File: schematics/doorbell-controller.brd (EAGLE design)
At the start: 114.3 x 100 mm, 7 parts, among them Q1 BC557

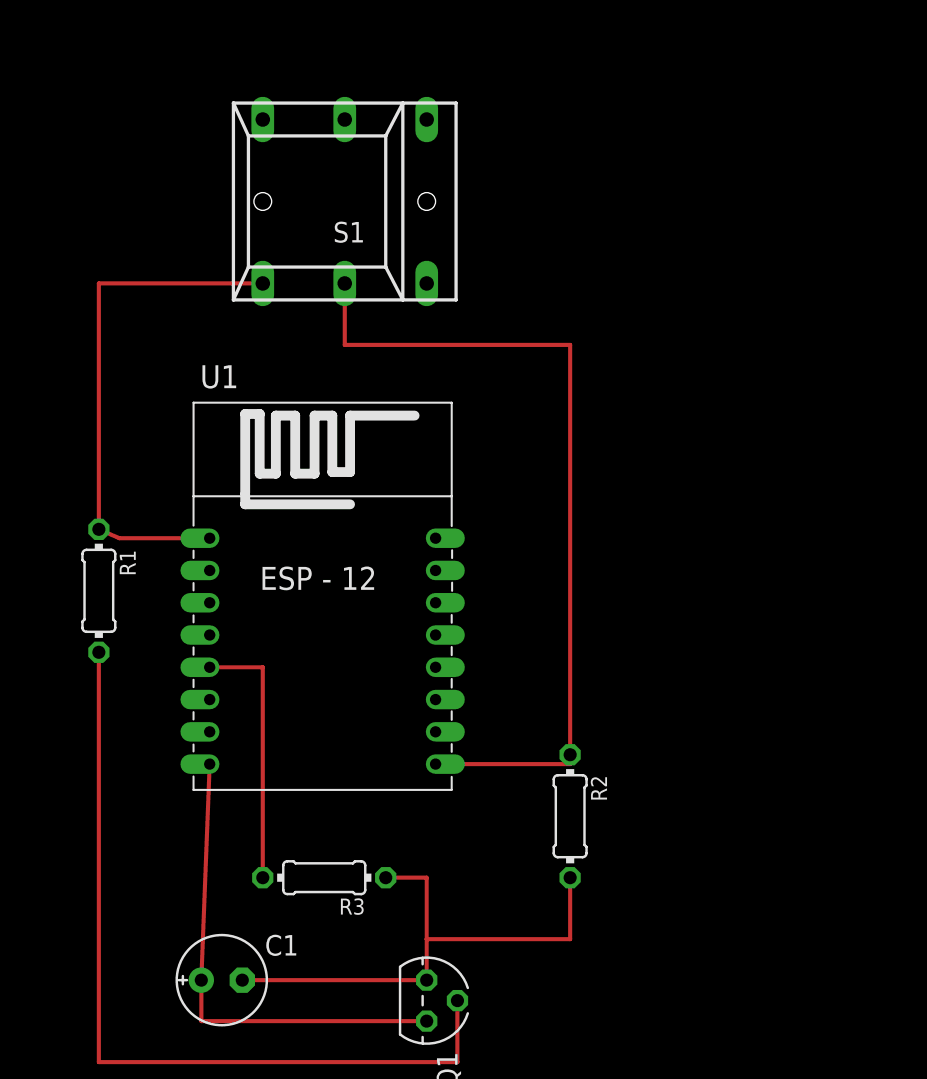
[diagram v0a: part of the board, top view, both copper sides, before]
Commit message: Added LEDs to schematics; Replaces button with Clamp
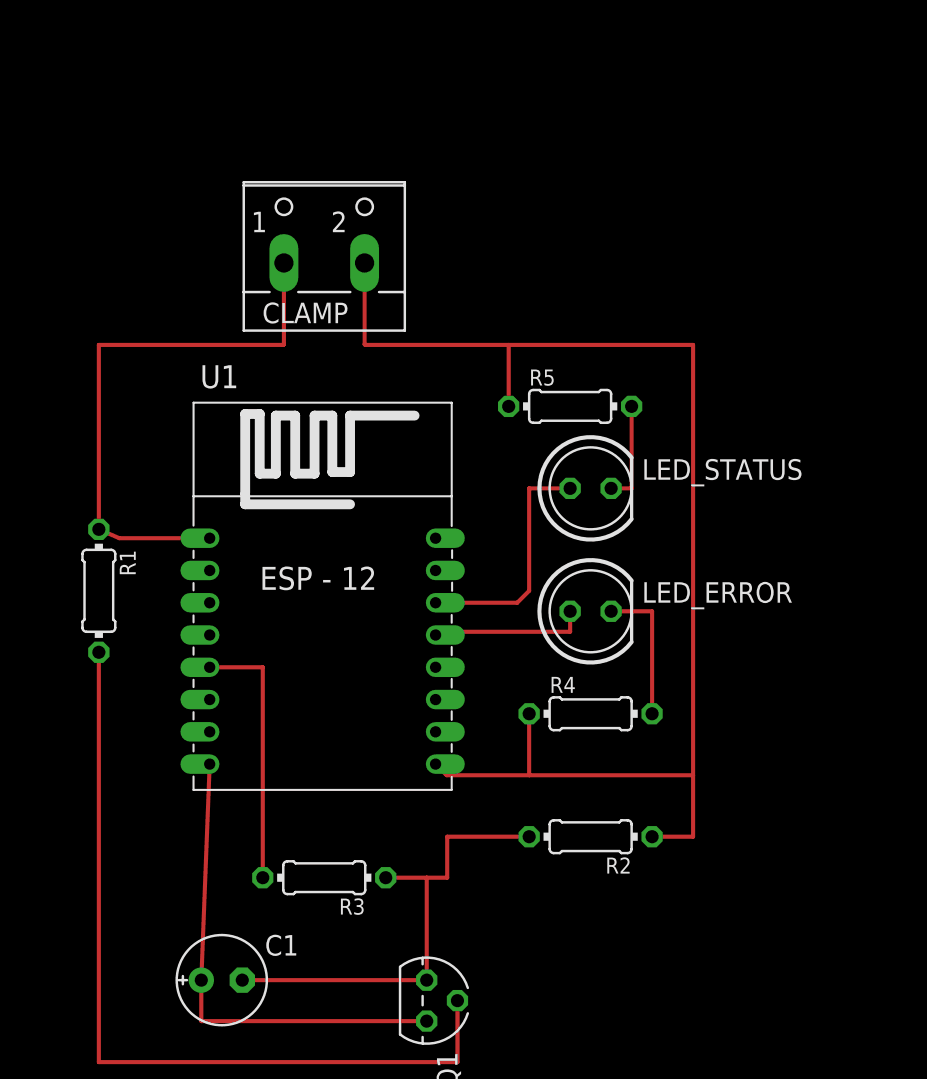
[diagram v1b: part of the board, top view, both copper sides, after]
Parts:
- removed S1: (no value), switch:REKN
- added CLAMP: (no value), con-wago-500:W237-102
- added LED_ERROR, LED_STATUS: (no value), led:LED5MM
- added R4, R5: 470, rcl:0204/7
- moved R2 1.80 mm to (66.0, 38.1), turned to 180 degrees
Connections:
- new net N$1: LED_STATUS.A, U1.GPIO5
- new net N$4: LED_ERROR.A, U1.GPIO4
- new net N$6: LED_ERROR.K, R4.2
- new net N$7: LED_STATUS.K, R5.2
- net GND: now also CLAMP.2, R4.1, R5.1; no longer S1.1A
- net RST: now also CLAMP.1; no longer S1.0A
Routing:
- net GND: track 52.1 -> 82.3 mm
- net N$1: track 0.00 -> 15.0 mm
- net N$4: track 0.00 -> 9.69 mm
- net N$6: track 0.00 -> 8.89 mm
- net N$7: track 0.00 -> 6.35 mm
- net N$5: track 33.0 -> 29.2 mm
- net RST: track 32.4 -> 34.9 mm
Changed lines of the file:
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@@
 <attribute name="SPICEPREFIX" value="R" x="35.56" y="53.34" size="1.778" layer="27" rot="R270" display="off"/>
 </element>
-<element name="R2" library="rcl" library_urn="urn:adsk.eagle:library:334" package="0204/7" package3d_urn="urn:adsk.eagle:package:23498/1" value="22k" x="64.77" y="39.37" rot="R270">
-<attribute name="SPICEPREFIX" value="R" x="64.77" y="39.37" size="1.778" layer="27" rot="R270" display="off"/>
+<element name="R2" library="rcl" library_urn="urn:adsk.eagle:library:334" package="0204/7" package3d_urn="urn:adsk.eagle:package:23498/1" value="22k" x="66.04" y="38.1" rot="R180">
+<attribute name="SPICEPREFIX" value="R" x="66.04" y="38.1" size="1.778" layer="27" rot="R180" display="off"/>
 </element>
 <element name="R3" library="rcl" library_urn="urn:adsk.eagle:library:334" package="0204/7" package3d_urn="urn:adsk.eagle:package:23498/1" value="470" x="49.53" y="35.56" rot="R180">
 <attribute name="SPICEPREFIX" value="R" x="49.53" y="35.56" size="1.778" layer="27" rot="R180" display="off"/>
 </element>
-<element name="S1" library="switch" library_urn="urn:adsk.eagle:library:380" package="REKN" package3d_urn="urn:adsk.eagle:package:27692/1" value="" x="50.8" y="77.47" rot="R180"/>
 <element name="U1" library="esp8266modules" package="ESP12-TR" value="" x="49.53" y="50.8"/>
+<element name="LED_STATUS" library="led" library_urn="urn:adsk.eagle:library:259" package="LED5MM" package3d_urn="urn:adsk.eagle:package:15799/2" value="" x="66.04" y="59.69"/>
+<element name="LED_ERROR" library="led" library_urn="urn:adsk.eagle:library:259" package="LED5MM" package3d_urn="urn:adsk.eagle:package:15799/2" value="" x="66.04" y="52.07"/>
+<element name="R4" library="rcl" library_urn="urn:adsk.eagle:library:334" package="0204/7" package3d_urn="urn:adsk.eagle:package:23498/1" value="470" x="66.04" y="45.72">
+<attribute name="SPICEPREFIX" value="R" x="66.04" y="45.72" size="1.778" layer="27" display="off"/>
+</element>
+<element name="R5" library="rcl" library_urn="urn:adsk.eagle:library:334" package="0204/7" package3d_urn="urn:adsk.eagle:package:23498/1" value="470" x="64.77" y="64.77">
+<attribute name="SPICEPREFIX" value="R" x="64.77" y="64.77" size="1.778" layer="27" display="off"/>
+</element>
+<element name="CLAMP" library="con-wago-500" library_urn="urn:adsk.eagle:library:195" package="W237-102" package3d_urn="urn:adsk.eagle:package:10688/1" value="" x="49.53" y="74.93">
+<attribute name="MF" value="" x="49.53" y="74.93" size="1.778" layer="27" display="off"/>
+<attribute name="MPN" value="237-102" x="49.53" y="74.93" size="1.778" layer="27" display="off"/>
+<attribute name="OC_FARNELL" value="unknown" x="49.53" y="74.93" size="1.778" layer="27" display="off"/>
+<attribute name="OC_NEWARK" value="70K9898" x="49.53" y="74.93" size="1.778" layer="27" display="off"/>
+</element>
 </elements>
 <signals>
 <signal name="GND">
-<contactref element="S1" pad="1A"/>
 <contactref element="R2" pad="1"/>
 <contactref element="U1" pad="GND"/>
-<wire x1="64.77" y1="43.18" x2="64.77" y2="42.6" width="0.254" layer="1"/>
-<wire x1="64.77" y1="42.6" x2="56.43" y2="42.6" width="0.254" layer="1"/>
-<wire x1="50.8" y1="72.39" x2="50.8" y2="68.58" width="0.254" layer="1"/>
-<wire x1="50.8" y1="68.58" x2="64.77" y2="68.58" width="0.254" layer="1"/>
-<wire x1="64.77" y1="68.58" x2="64.77" y2="43.18" width="0.254" layer="1"/>
+<contactref element="R4" pad="1"/>
+<contactref element="R5" pad="1"/>
+<wire x1="60.96" y1="68.58" x2="72.39" y2="68.58" width="0.254" layer="1"/>
+<wire x1="60.96" y1="64.77" x2="60.96" y2="68.58" width="0.254" layer="1"/>
+<wire x1="72.39" y1="68.58" x2="72.39" y2="41.91" width="0.254" layer="1"/>
+<wire x1="62.23" y1="41.91" x2="57.12" y2="41.91" width="0.254" layer="1"/>
+<wire x1="57.12" y1="41.91" x2="56.43" y2="42.6" width="0.254" layer="1"/>
+<wire x1="62.23" y1="45.72" x2="62.23" y2="41.91" width="0.254" layer="1"/>
+<wire x1="62.23" y1="41.91" x2="72.39" y2="41.91" width="0.254" layer="1"/>
+<wire x1="69.85" y1="38.1" x2="72.39" y2="38.1" width="0.254" layer="1"/>
+<wire x1="72.39" y1="38.1" x2="72.39" y2="41.91" width="0.254" layer="1"/>
+<contactref element="CLAMP" pad="2"/>
+<wire x1="52.03" y1="73.66" x2="52.03" y2="68.62" width="0.254" layer="1"/>
+<wire x1="52.03" y1="68.62" x2="52.07" y2="68.58" width="0.254" layer="1"/>
+<wire x1="52.07" y1="68.58" x2="60.96" y2="68.58" width="0.254" layer="1"/>
 </signal>
 <signal name="N$5">
@@
 <contactref element="R3" pad="1"/>
 <wire x1="53.34" y1="35.56" x2="55.88" y2="35.56" width="0.254" layer="1"/>
-<wire x1="55.88" y1="29.21" x2="55.88" y2="31.75" width="0.254" layer="1"/>
-<wire x1="55.88" y1="31.75" x2="55.88" y2="35.56" width="0.254" layer="1"/>
+<wire x1="55.88" y1="29.21" x2="55.88" y2="35.56" width="0.254" layer="1"/>
 <wire x1="55.88" y1="29.21" x2="44.45" y2="29.21" width="0.254" layer="1"/>
-<wire x1="64.77" y1="35.56" x2="64.77" y2="31.75" width="0.254" layer="1"/>
-<wire x1="64.77" y1="31.75" x2="55.88" y2="31.75" width="0.254" layer="1"/>
+<wire x1="55.88" y1="35.56" x2="57.15" y2="35.56" width="0.254" layer="1"/>
+<wire x1="57.15" y1="35.56" x2="57.15" y2="38.1" width="0.254" layer="1"/>
+<wire x1="57.15" y1="38.1" x2="62.23" y2="38.1" width="0.254" layer="1"/>
 </signal>
 <signal name="N$8">
@@
 <contactref element="R1" pad="1"/>
 <contactref element="U1" pad="RST"/>
-<contactref element="S1" pad="0A"/>
 <wire x1="35.56" y1="57.15" x2="36.83" y2="56.6" width="0.254" layer="1"/>
 <wire x1="36.83" y1="56.6" x2="42.43" y2="56.6" width="0.254" layer="1"/>
-<wire x1="35.56" y1="57.15" x2="35.56" y2="72.39" width="0.254" layer="1"/>
-<wire x1="35.56" y1="72.39" x2="45.72" y2="72.39" width="0.254" layer="1"/>
+<wire x1="35.56" y1="57.15" x2="35.56" y2="68.58" width="0.254" layer="1"/>
+<contactref element="CLAMP" pad="1"/>
+<wire x1="35.56" y1="68.58" x2="35.56" y2="72.39" width="0" layer="19" extent="1-16"/>
+<wire x1="47.03" y1="73.66" x2="47.03" y2="68.62" width="0.254" layer="1"/>
+<wire x1="47.03" y1="68.62" x2="46.99" y2="68.58" width="0.254" layer="1"/>
+<wire x1="46.99" y1="68.58" x2="35.56" y2="68.58" width="0.254" layer="1"/>
 </signal>
 <signal name="N$3">
@@
 <wire x1="45.72" y1="35.56" x2="45.72" y2="48.6" width="0.254" layer="1"/>
 </signal>
+<signal name="N$1">
+<contactref element="U1" pad="GPIO5"/>
+<contactref element="LED_STATUS" pad="A"/>
+<wire x1="64.77" y1="59.69" x2="62.23" y2="59.69" width="0.254" layer="1"/>
+<wire x1="62.23" y1="59.69" x2="62.23" y2="53.34" width="0.254" layer="1"/>
+<wire x1="62.23" y1="53.34" x2="61.49" y2="52.6" width="0.254" layer="1"/>
+<wire x1="61.49" y1="52.6" x2="56.43" y2="52.6" width="0.254" layer="1"/>
+</signal>
+<signal name="N$4">
+<contactref element="U1" pad="GPIO4"/>
+<contactref element="LED_ERROR" pad="A"/>
+<wire x1="64.77" y1="52.07" x2="64.77" y2="50.8" width="0.254" layer="1"/>
+<wire x1="64.77" y1="50.8" x2="56.63" y2="50.8" width="0.254" layer="1"/>
+<wire x1="56.63" y1="50.8" x2="56.43" y2="50.6" width="0.254" layer="1"/>
+</signal>
+<signal name="N$6">
+<contactref element="LED_ERROR" pad="K"/>
+<contactref element="R4" pad="2"/>
+<wire x1="67.31" y1="52.07" x2="69.85" y2="52.07" width="0.254" layer="1"/>
+<wire x1="69.85" y1="52.07" x2="69.85" y2="45.72" width="0.254" layer="1"/>
+</signal>
+<signal name="N$7">
+<contactref element="R5" pad="2"/>
+<contactref element="LED_STATUS" pad="K"/>
+<wire x1="67.31" y1="59.69" x2="68.58" y2="59.69" width="0.254" layer="1"/>
+<wire x1="68.58" y1="59.69" x2="68.58" y2="64.77" width="0.254" layer="1"/>
+</signal>
 </signals>

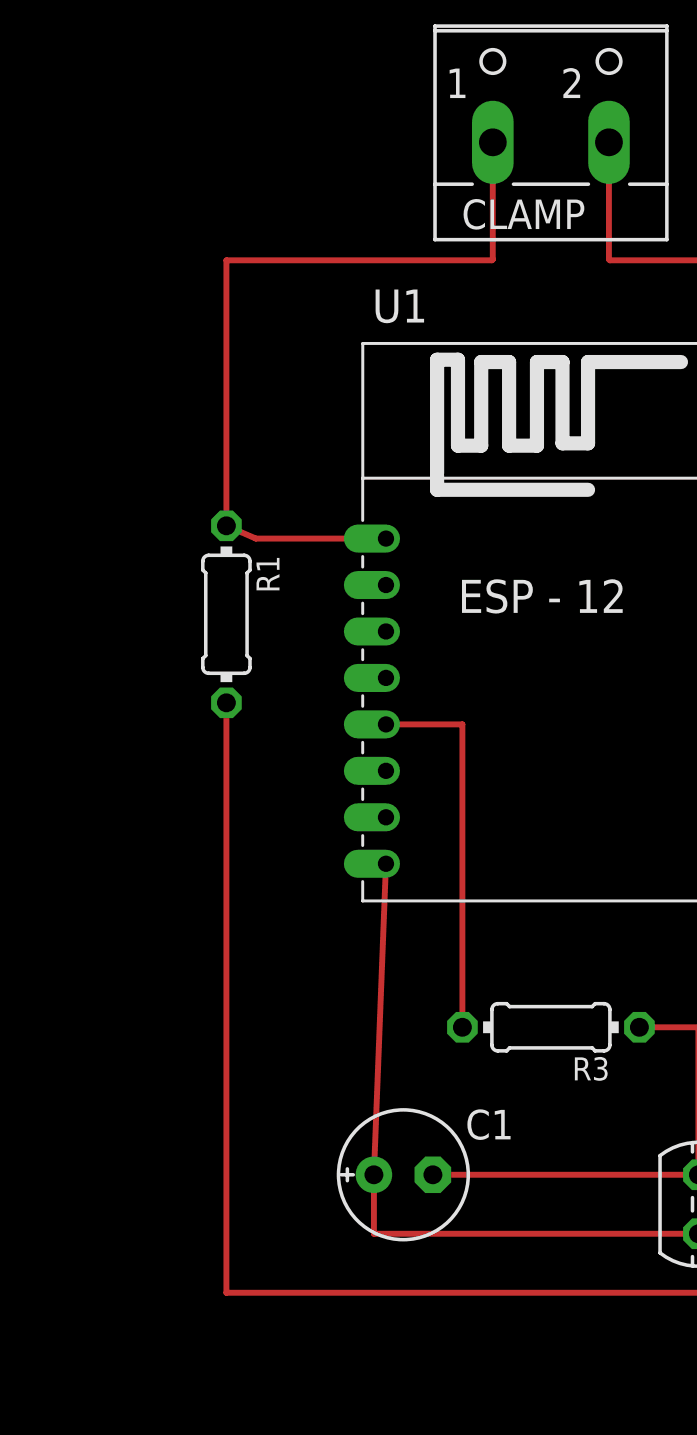
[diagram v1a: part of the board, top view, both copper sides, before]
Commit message: Hooked up RST to GPIO16
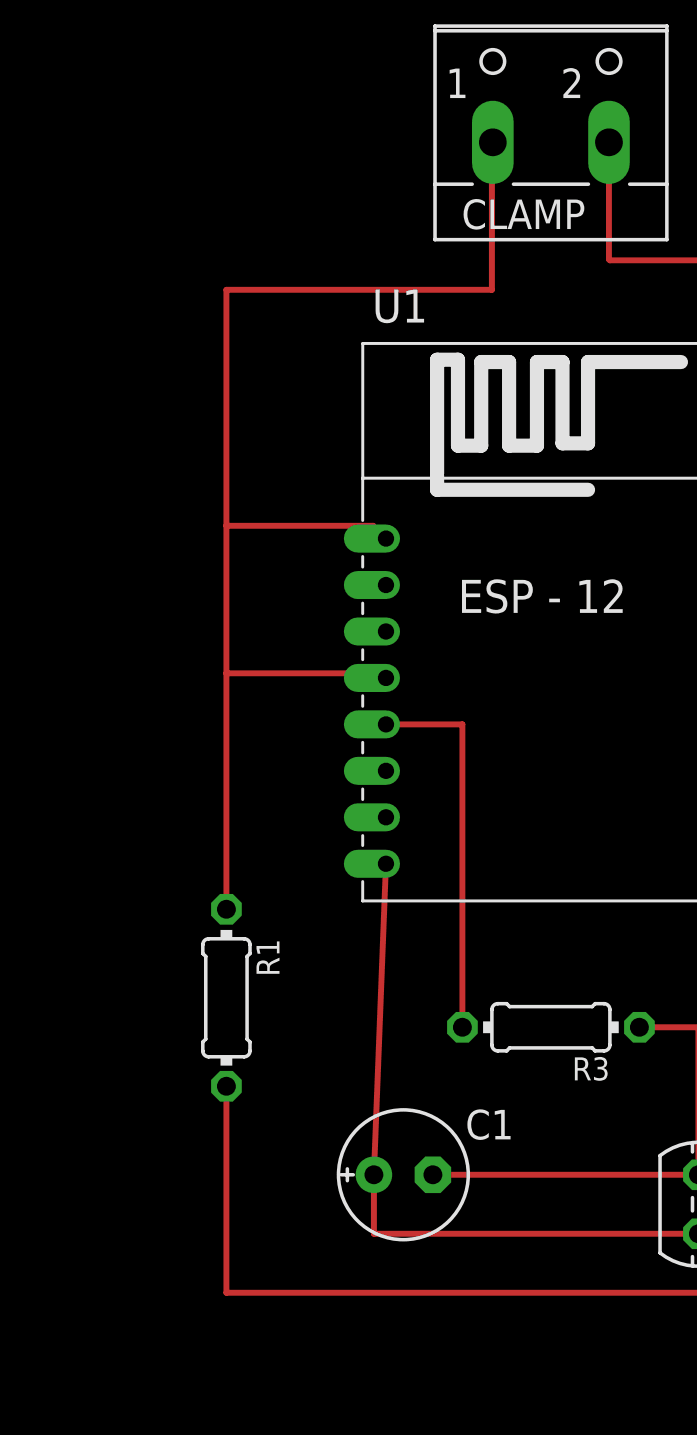
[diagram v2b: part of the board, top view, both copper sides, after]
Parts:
- moved R1 16.5 mm to (35.6, 36.8)
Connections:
- net RST: now also U1.GPIO16
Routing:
- net RST: track 34.9 -> 58.5 mm
- net N$2: track 51.4 -> 34.9 mm
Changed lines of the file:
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@@
 </element>
 <element name="Q1" library="transistor-pnp" library_urn="urn:adsk.eagle:library:399" package="TO92" package3d_urn="urn:adsk.eagle:package:29211/2" value="BC557" x="55.88" y="27.94" rot="R270"/>
-<element name="R1" library="rcl" library_urn="urn:adsk.eagle:library:334" package="0204/7" package3d_urn="urn:adsk.eagle:package:23498/1" value="22k" x="35.56" y="53.34" rot="R270">
-<attribute name="SPICEPREFIX" value="R" x="35.56" y="53.34" size="1.778" layer="27" rot="R270" display="off"/>
+<element name="R1" library="rcl" library_urn="urn:adsk.eagle:library:334" package="0204/7" package3d_urn="urn:adsk.eagle:package:23498/1" value="22k" x="35.56" y="36.83" rot="R270">
+<attribute name="SPICEPREFIX" value="R" x="35.56" y="36.83" size="1.778" layer="27" rot="R270" display="off"/>
 </element>
 <element name="R2" library="rcl" library_urn="urn:adsk.eagle:library:334" package="0204/7" package3d_urn="urn:adsk.eagle:package:23498/1" value="22k" x="66.04" y="38.1" rot="R180">
@@
 <wire x1="57.785" y1="27.94" x2="57.785" y2="24.13" width="0.254" layer="1"/>
 <wire x1="35.56" y1="24.13" x2="57.785" y2="24.13" width="0.254" layer="1"/>
-<wire x1="35.56" y1="49.53" x2="35.56" y2="24.13" width="0.254" layer="1"/>
+<wire x1="35.56" y1="33.02" x2="35.56" y2="24.13" width="0.254" layer="1"/>
 </signal>
 <signal name="RST">
 <contactref element="R1" pad="1"/>
 <contactref element="U1" pad="RST"/>
-<wire x1="35.56" y1="57.15" x2="36.83" y2="56.6" width="0.254" layer="1"/>
-<wire x1="36.83" y1="56.6" x2="42.43" y2="56.6" width="0.254" layer="1"/>
-<wire x1="35.56" y1="57.15" x2="35.56" y2="68.58" width="0.254" layer="1"/>
 <contactref element="CLAMP" pad="1"/>
-<wire x1="35.56" y1="68.58" x2="35.56" y2="72.39" width="0" layer="19" extent="1-16"/>
-<wire x1="47.03" y1="73.66" x2="47.03" y2="68.62" width="0.254" layer="1"/>
-<wire x1="47.03" y1="68.62" x2="46.99" y2="68.58" width="0.254" layer="1"/>
-<wire x1="46.99" y1="68.58" x2="35.56" y2="68.58" width="0.254" layer="1"/>
+<wire x1="35.56" y1="40.64" x2="35.56" y2="50.8" width="0.254" layer="1"/>
+<wire x1="35.56" y1="50.8" x2="35.56" y2="57.15" width="0.254" layer="1"/>
+<wire x1="35.56" y1="57.15" x2="35.56" y2="67.31" width="0.254" layer="1"/>
+<wire x1="35.56" y1="67.31" x2="46.99" y2="67.31" width="0.254" layer="1"/>
+<wire x1="46.99" y1="67.31" x2="46.99" y2="73.62" width="0.254" layer="1"/>
+<wire x1="46.99" y1="73.62" x2="47.03" y2="73.66" width="0.254" layer="1"/>
+<contactref element="U1" pad="GPIO16"/>
+<wire x1="42.43" y1="56.6" x2="41.88" y2="57.15" width="0.254" layer="1"/>
+<wire x1="41.88" y1="57.15" x2="35.56" y2="57.15" width="0.254" layer="1"/>
+<wire x1="42.43" y1="50.6" x2="42.23" y2="50.8" width="0.254" layer="1"/>
+<wire x1="42.23" y1="50.8" x2="35.56" y2="50.8" width="0.254" layer="1"/>
 </signal>
 <signal name="N$3">
